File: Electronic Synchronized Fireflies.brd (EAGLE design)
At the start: 37 x 29 mm, 30 parts, among them Q1 BSS123, Q2 BSS84, Q3 LPT80A, Q4 LPT80A, Q5 LPT80A, U1 NCP1400A, U2 MSP430G2231

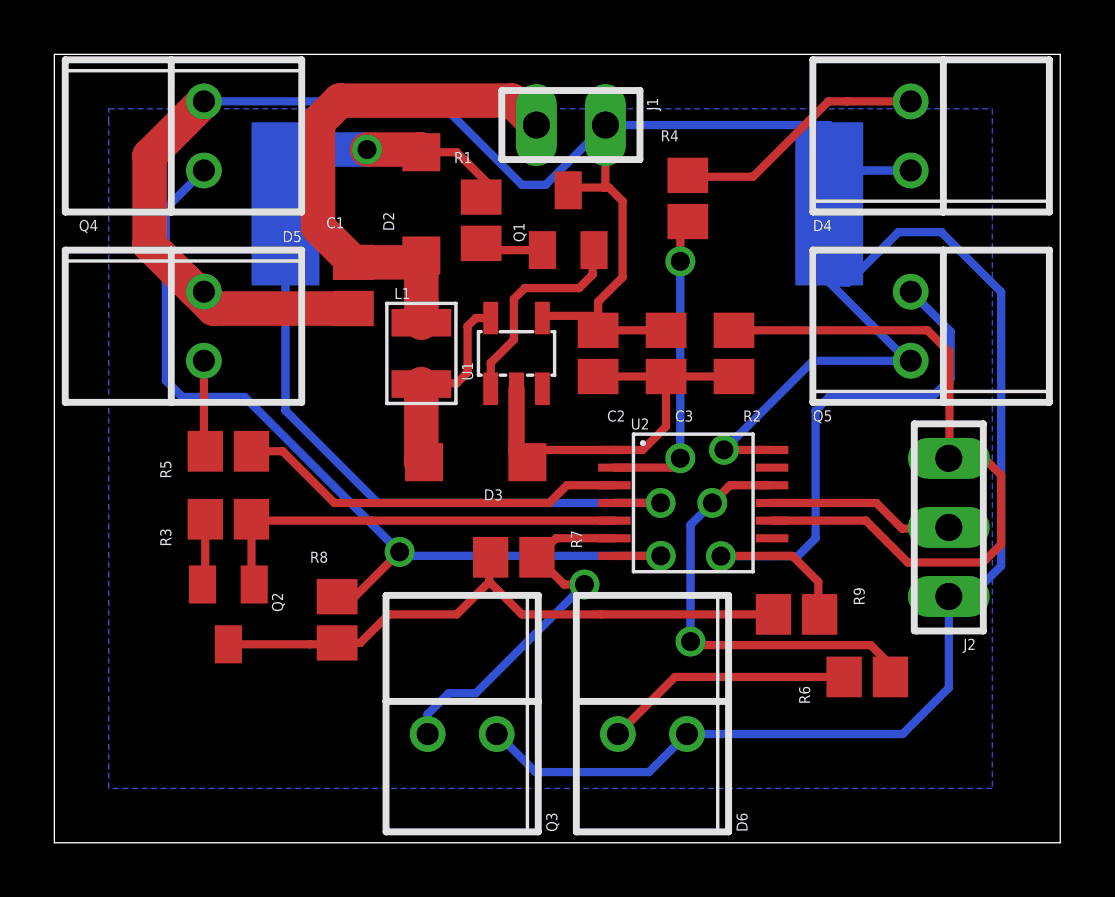
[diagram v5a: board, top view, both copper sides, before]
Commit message: Fixed battery lines covered by solar cell. Added labels.
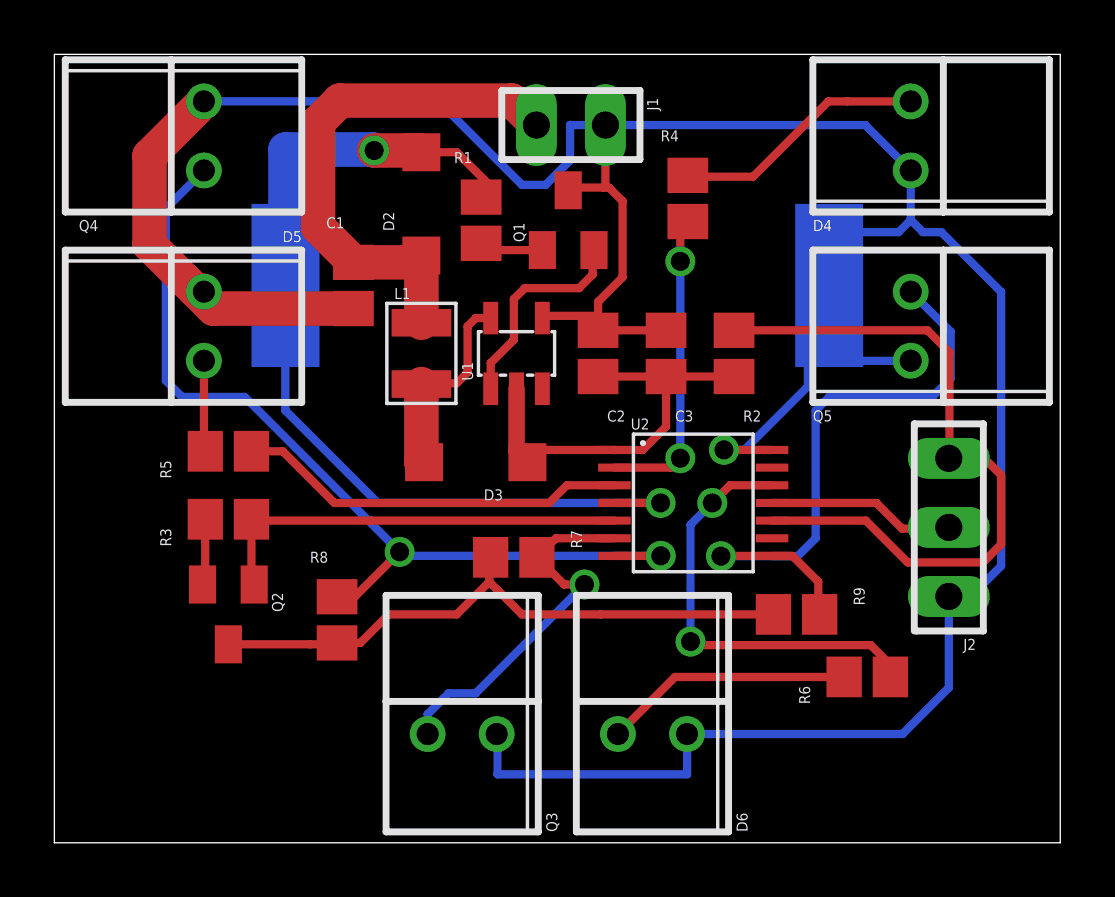
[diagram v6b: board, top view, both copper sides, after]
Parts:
- moved D1 3.00 mm to (18.5, 20.5)
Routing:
- net GND: track 119.0 -> 122.4 mm
- removed copper zone on layer 16, net GND
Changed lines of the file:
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@@
 <setting verticaltext="up"/>
 </settings>
-<grid distance="0.5" unitdist="mm" unit="mm" style="lines" multiple="1" display="yes" altdistance="0.025" altunitdist="inch" altunit="inch"/>
+<grid distance="0.003125" unitdist="mic" unit="mm" style="lines" multiple="1" display="yes" altdistance="0.025" altunitdist="inch" altunit="inch"/>
 <layers>
 <layer number="1" name="Top" color="4" fill="1" visible="yes" active="yes"/>
@@
 </autorouter>
 <elements>
-<element name="D1" library="Electronic Synchronized Fireflies" package="KXOB22-04X3" value="KXOB22-04X3" x="18.5" y="23.5" rot="MR180"/>
+<element name="D1" library="Electronic Synchronized Fireflies" package="KXOB22-04X3" value="KXOB22-04X3" x="18.5" y="20.5" rot="MR180"/>
 <element name="D2" library="Electronic Synchronized Fireflies" package="SOD123" value="MBR0520LT" x="13.5" y="23.5" rot="R90"/>
 <element name="J1" library="Electronic Synchronized Fireflies" package="2WIRE_HEADER" value="" x="19" y="26.4" rot="R180">
@@
 <element name="C2" library="Electronic Synchronized Fireflies" package="CAPACITOR_0805" value="47uF" x="20" y="18" rot="R90"/>
 <element name="L1" library="Electronic Synchronized Fireflies" package="INDUCTOR_1007" value="22uH" x="13.5" y="18" rot="R270"/>
-<element name="Q1" library="Electronic Synchronized Fireflies" package="SOT23" value="BSS123" x="18.9" y="22.9"/>
+<element name="Q1" library="Electronic Synchronized Fireflies" package="SOT23" value="BSS123" x="18.9" y="22.9" smashed="yes">
+<attribute name="NAME" x="17.295" y="22.095" size="0.4064" layer="25" rot="R90"/>
+</element>
 <element name="R1" library="Electronic Synchronized Fireflies" package="RESISTOR_0805" value="20kR" x="15.7" y="22.9" rot="R270"/>
 <element name="U2" library="Electronic Synchronized Fireflies" package="TSSOP-14" value="MSP430G2231" x="23.5" y="12.5" rot="R270"/>
@@
 <attribute name="OC_FARNELL" value="1462950" x="32.9" y="11.6" size="1.778" layer="27" rot="R90" display="off"/>
 </element>
-<element name="Q2" library="Electronic Synchronized Fireflies" package="SOT23" value="BSS84" x="6.4" y="8.4" rot="R180"/>
+<element name="Q2" library="Electronic Synchronized Fireflies" package="SOT23" value="BSS84" x="6.4" y="8.4" smashed="yes" rot="R180">
+<attribute name="NAME" x="8.005" y="9.205" size="0.4064" layer="25" rot="R270"/>
+</element>
 <element name="R3" library="Electronic Synchronized Fireflies" package="RESISTOR_0805" value="20kR" x="6.4" y="11.9"/>
 <element name="R4" library="Electronic Synchronized Fireflies" package="RESISTOR_0805" value="56R" x="23.3" y="23.7" rot="R270"/>
@@
 <wire x1="20" y1="18.85" x2="20" y2="19.382765625" width="0.3048" layer="1"/>
 <wire x1="20" y1="19.382765625" x2="20" y2="19.6" width="0.3048" layer="1"/>
-<wire x1="28.5" y1="23.5" x2="29.73" y2="24.73" width="0.3048" layer="16"/>
-<wire x1="29.73" y1="24.73" x2="31.5" y2="24.73" width="0.3048" layer="16"/>
 <wire x1="17.95" y1="19.3001" x2="17.95" y2="19.75" width="0.3048" layer="1"/>
 <wire x1="22.5" y1="18.85" x2="22.8741" y2="19.2241" width="0.3048" layer="1"/>
@@
 <wire x1="17.95" y1="19.382765625" x2="20" y2="19.382765625" width="0.3048" layer="1"/>
 <wire x1="16.27" y1="4" x2="16.3" y2="4" width="0.3048" layer="16"/>
-<wire x1="16.3" y1="4" x2="17.7" y2="2.6" width="0.3048" layer="16"/>
-<wire x1="17.7" y1="2.6" x2="21.87" y2="2.6" width="0.3048" layer="16"/>
-<wire x1="21.87" y1="2.6" x2="23.27" y2="4" width="0.3048" layer="16"/>
 <wire x1="23.27" y1="4" x2="31.2" y2="4" width="0.3048" layer="16"/>
 <wire x1="31.2" y1="4" x2="32.9" y2="5.7" width="0.3048" layer="16"/>
 <wire x1="32.9" y1="5.7" x2="32.9" y2="9.06" width="0.3048" layer="16"/>
-<wire x1="28.5" y1="23.5" x2="28.5" y2="26.4" width="0.3048" layer="16"/>
-<wire x1="28.5" y1="26.4" x2="20.27" y2="26.4" width="0.3048" layer="16"/>
 <wire x1="5.5" y1="27.27" x2="14.13" y2="27.27" width="0.3048" layer="16"/>
 <wire x1="14.13" y1="27.27" x2="17.2" y2="24.2" width="0.3048" layer="16"/>
 <wire x1="17.2" y1="24.2" x2="18.07" y2="24.2" width="0.3048" layer="16"/>
-<wire x1="18.07" y1="24.2" x2="20.27" y2="26.4" width="0.3048" layer="16"/>
 <wire x1="5.5" y1="20.3" x2="5.2" y2="20.3" width="1.27" layer="1"/>
 <wire x1="5.2" y1="20.3" x2="4.8" y2="20.7" width="1.27" layer="1"/>
@@
 <wire x1="5.5" y1="20.3" x2="5.5" y2="20.27" width="1.27" layer="1"/>
 <wire x1="31.5" y1="17.73" x2="31.383721875" y2="17.73" width="0.3048" layer="16"/>
-<wire x1="31.383721875" y1="17.73" x2="28.504625" y2="20.609096875" width="0.3048" layer="16"/>
-<wire x1="28.504625" y1="20.609096875" x2="29.1987375" y2="20.609096875" width="0.3048" layer="16"/>
-<wire x1="29.1987375" y1="20.609096875" x2="31.049940625" y2="22.4603" width="0.3048" layer="16"/>
-<wire x1="31.049940625" y1="22.4603" x2="32.626221875" y2="22.4603" width="0.3048" layer="16"/>
+<wire x1="28.504625" y1="20.609096875" x2="29.0085" y2="20.609096875" width="0.3048" layer="16"/>
+<wire x1="29.0085" y1="20.609096875" x2="29.1987375" y2="20.609096875" width="0.3048" layer="16"/>
 <wire x1="32.626221875" y1="22.4603" x2="34.824525" y2="20.261996875" width="0.3048" layer="16"/>
 <wire x1="34.824525" y1="20.261996875" x2="34.824525" y2="10.181578125" width="0.3048" layer="16"/>
@@
 <wire x1="24.632140625" y1="14.4499" x2="24.6293" y2="14.452740625" width="0.3048" layer="1"/>
 <via x="24.6293" y="14.452740625" extent="1-16" drill="0.7"/>
-<wire x1="24.6293" y1="14.452740625" x2="27.906559375" y2="17.73" width="0.3048" layer="16"/>
 <wire x1="27.906559375" y1="17.73" x2="31.5" y2="17.73" width="0.3048" layer="16"/>
-<polygon width="1.016" layer="16">
-<vertex x="2" y="27"/>
-<vertex x="34.5" y="27"/>
-<vertex x="34.5" y="2"/>
-<vertex x="2" y="2"/>
-<vertex x="2" y="26.5"/>
-</polygon>
+<wire x1="20.27" y1="26.4" x2="29.83" y2="26.4" width="0.3048" layer="16"/>
+<wire x1="29.83" y1="26.4" x2="31.5" y2="24.73" width="0.3048" layer="16"/>
+<wire x1="31.5" y1="24.73" x2="31.5" y2="22.910359375" width="0.3048" layer="16"/>
+<wire x1="32.626221875" y1="22.4603" x2="31.950059375" y2="22.4603" width="0.3048" layer="16"/>
+<wire x1="31.950059375" y1="22.4603" x2="31.5" y2="22.910359375" width="0.3048" layer="16"/>
+<wire x1="28.504625" y1="20.609096875" x2="28.504625" y2="20.504625" width="0.3048" layer="16"/>
+<wire x1="28.504625" y1="20.504625" x2="28.5" y2="20.5" width="0.3048" layer="16"/>
+<wire x1="16.3" y1="4" x2="16.3" y2="2.518978125" width="0.3048" layer="16"/>
+<wire x1="16.3" y1="2.518978125" x2="23.27355625" y2="2.518978125" width="0.3048" layer="16"/>
+<wire x1="23.27355625" y1="2.518978125" x2="23.27355625" y2="4" width="0.3048" layer="16"/>
+<wire x1="23.27355625" y1="4" x2="23.27" y2="4" width="0.3048" layer="16"/>
+<wire x1="31.5" y1="22.910359375" x2="31.0508" y2="22.461159375" width="0.3048" layer="16"/>
+<wire x1="31.0508" y1="22.461159375" x2="29.245796875" y2="22.461159375" width="0.3048" layer="16"/>
+<wire x1="29.245796875" y1="22.461159375" x2="29.0085" y2="22.2238625" width="0.3048" layer="16"/>
+<wire x1="29.0085" y1="22.2238625" x2="29.0085" y2="20.609096875" width="0.3048" layer="16"/>
+<wire x1="28.5" y1="20.5" x2="27.71816875" y2="19.71816875" width="0.3048" layer="16"/>
+<wire x1="27.71816875" y1="19.71816875" x2="27.71816875" y2="18.330271875" width="0.3048" layer="16"/>
+<wire x1="27.71816875" y1="18.330271875" x2="27.71816875" y2="16.787684375" width="0.3048" layer="16"/>
+<wire x1="27.71816875" y1="16.787684375" x2="25.383225" y2="14.452740625" width="0.3048" layer="16"/>
+<wire x1="25.383225" y1="14.452740625" x2="24.6293" y2="14.452740625" width="0.3048" layer="16"/>
+<wire x1="27.906559375" y1="17.73" x2="27.71816875" y2="17.918390625" width="0.3048" layer="16"/>
+<wire x1="27.71816875" y1="17.918390625" x2="27.71816875" y2="18.330271875" width="0.3048" layer="16"/>
+<wire x1="18.07" y1="24.2" x2="18.96886875" y2="25.09886875" width="0.3048" layer="16"/>
+<wire x1="18.96886875" y1="25.09886875" x2="18.96886875" y2="26.40475" width="0.3048" layer="16"/>
+<wire x1="18.96886875" y1="26.40475" x2="18.97361875" y2="26.4" width="0.3048" layer="16"/>
+<wire x1="18.97361875" y1="26.4" x2="20.27" y2="26.4" width="0.3048" layer="16"/>
 </signal>
 <signal name="N$1">
@@
 <contactref element="R1" pad="1"/>
 <contactref element="U2" pad="4"/>
-<wire x1="13.5" y1="25.4" x2="13.5" y2="25.5" width="1.27" layer="1"/>
-<wire x1="13.5" y1="25.5" x2="11.5" y2="25.5" width="1.27" layer="1"/>
-<via x="11.5" y="25.5" extent="1-16" drill="0.7"/>
-<wire x1="11.5" y1="25.5" x2="8.5" y2="25.5" width="1.27" layer="16"/>
-<wire x1="8.5" y1="25.5" x2="8.5" y2="23.5" width="1.27" layer="16"/>
+<wire x1="8.5" y1="25.5" x2="8.5" y2="20.5" width="1.27" layer="16"/>
 <wire x1="15.7" y1="23.75" x2="16" y2="24.2" width="0.3048" layer="1"/>
 <wire x1="20.5999" y1="12.5" x2="22.3" y2="12.5" width="0.3048" layer="1"/>
@@
 <wire x1="22.3" y1="12.5" x2="11.9" y2="12.5" width="0.3048" layer="16"/>
 <wire x1="11.9" y1="12.5" x2="8.5" y2="15.9" width="0.3048" layer="16"/>
-<wire x1="8.5" y1="15.9" x2="8.5" y2="23.5" width="0.3048" layer="16"/>
 <wire x1="13.5" y1="25.4" x2="14.8" y2="25.4" width="0.3048" layer="1"/>
 <wire x1="14.8" y1="25.4" x2="16" y2="24.2" width="0.3048" layer="1"/>
+<wire x1="13.5" y1="25.4" x2="13.4352625" y2="25.4647375" width="1.27" layer="1"/>
+<wire x1="13.4352625" y1="25.4647375" x2="11.76214375" y2="25.4647375" width="1.27" layer="1"/>
+<via x="11.76214375" y="25.4647375" extent="1-16" drill="0.7"/>
+<wire x1="11.76214375" y1="25.4647375" x2="11.72688125" y2="25.5" width="1.27" layer="16"/>
+<wire x1="11.72688125" y1="25.5" x2="8.5" y2="25.5" width="1.27" layer="16"/>
+<wire x1="8.5" y1="15.9" x2="8.5" y2="20.5" width="0.3048" layer="16"/>
 </signal>
 <signal name="N$3">

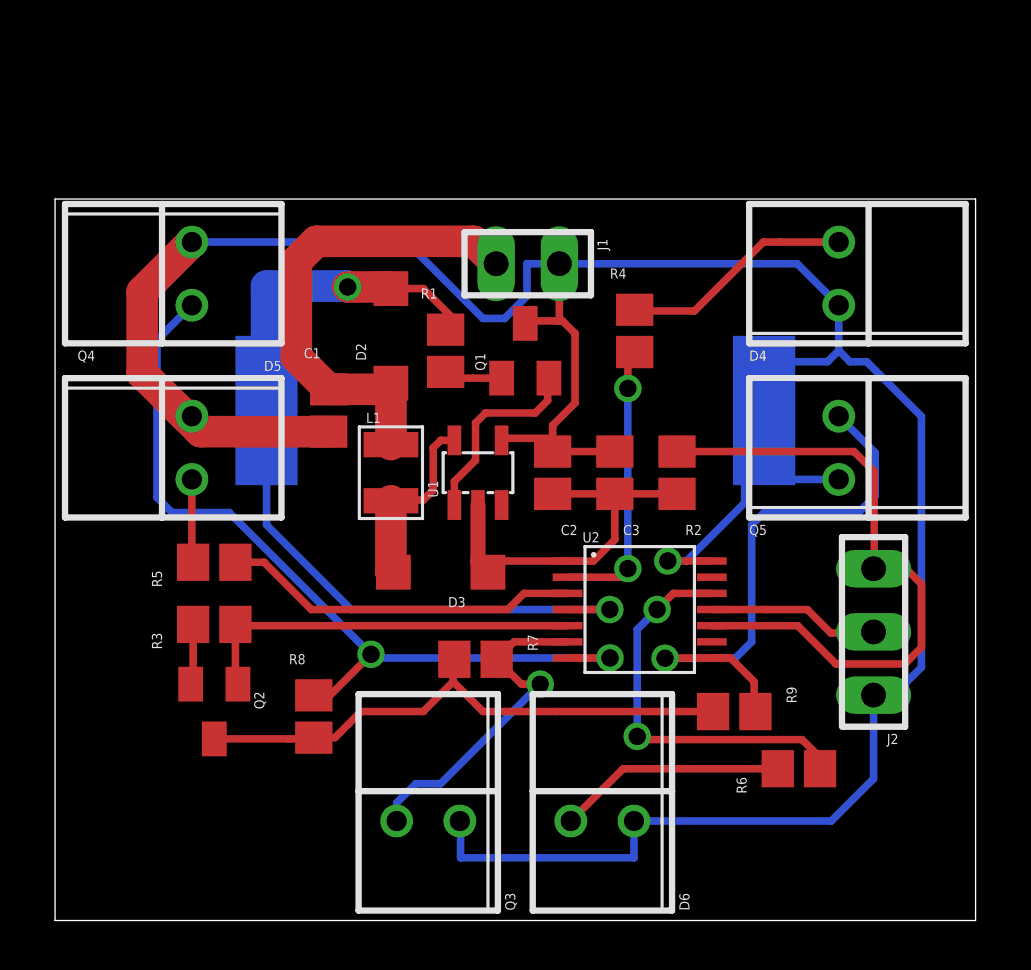
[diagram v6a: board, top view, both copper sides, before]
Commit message: Added drill holes, ground plane, octagon board
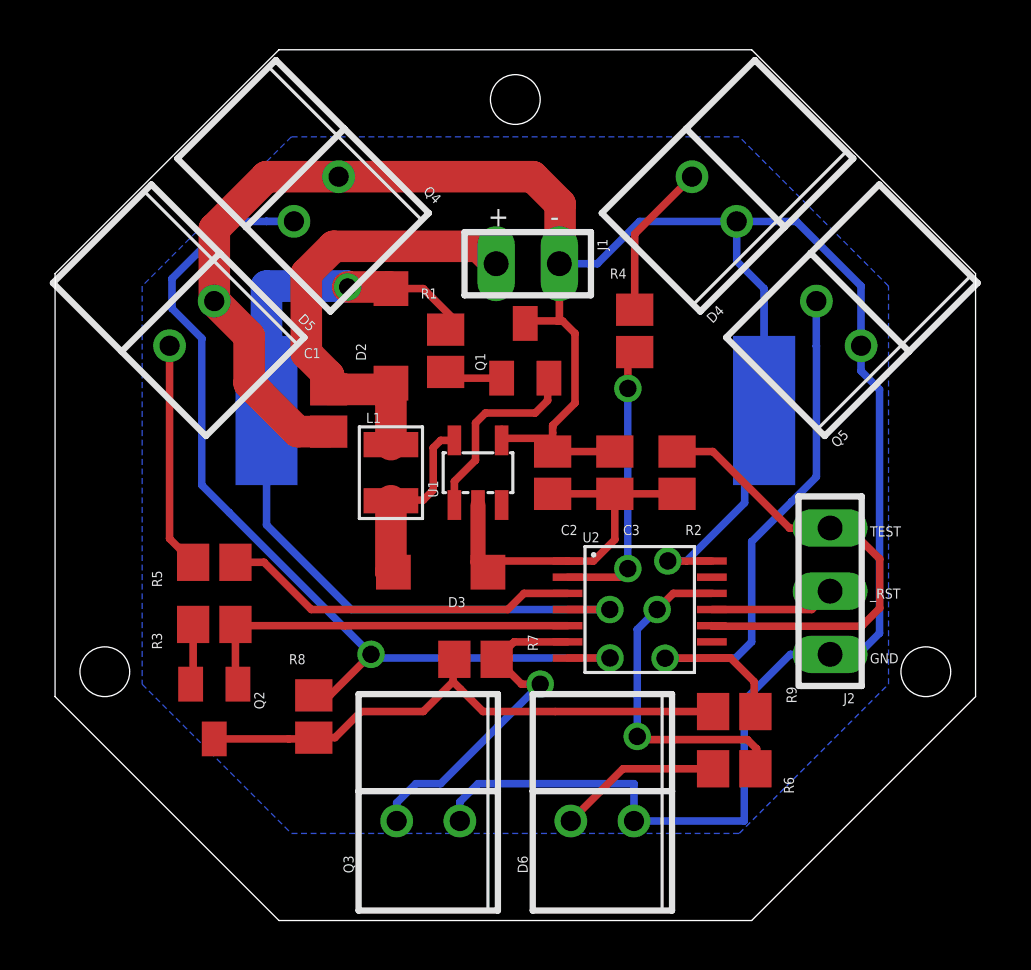
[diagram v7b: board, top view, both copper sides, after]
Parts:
- moved D4 5.83 mm to (26.5, 29.0), turned to 315 degrees
- moved Q4 5.83 mm to (10.5, 29.0), turned to 45 degrees
- moved D5 5.00 mm to (5.50, 24.0), turned to 45 degrees
- moved Q5 5.00 mm to (31.5, 24.0), turned to 315 degrees
- moved R6 2.60 mm to (27.3, 6.10)
- moved J2 2.39 mm to (31.2, 13.2)
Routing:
- net N$9: track 26.2 -> 19.0 mm
- net GND: track 122.4 -> 116.1 mm
- net N$20: track 3.35 -> 9.17 mm
- net N$13: track 34.2 -> 39.0 mm
- net N$22: track 9.37 -> 6.30 mm
- net N$21: track 9.19 -> 6.59 mm
- net N$18: track 16.1 -> 13.7 mm
- net N$11: track 6.91 -> 5.06 mm
- net N$1: track 19.6 -> 18.6 mm
- net N$15: track 23.7 -> 24.5 mm
- added copper zone on layer 16, net GND
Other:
- board size 37 x 29 mm -> 37 x 35 mm
- board text added: "+"
- board text added: "-"
- board text added: "GND"
- board text added: "TEST"
- board text added: "_RST"
